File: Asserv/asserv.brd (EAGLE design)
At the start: 44.1 x 57.1 mm, 8 parts, among them IC1 7805TV

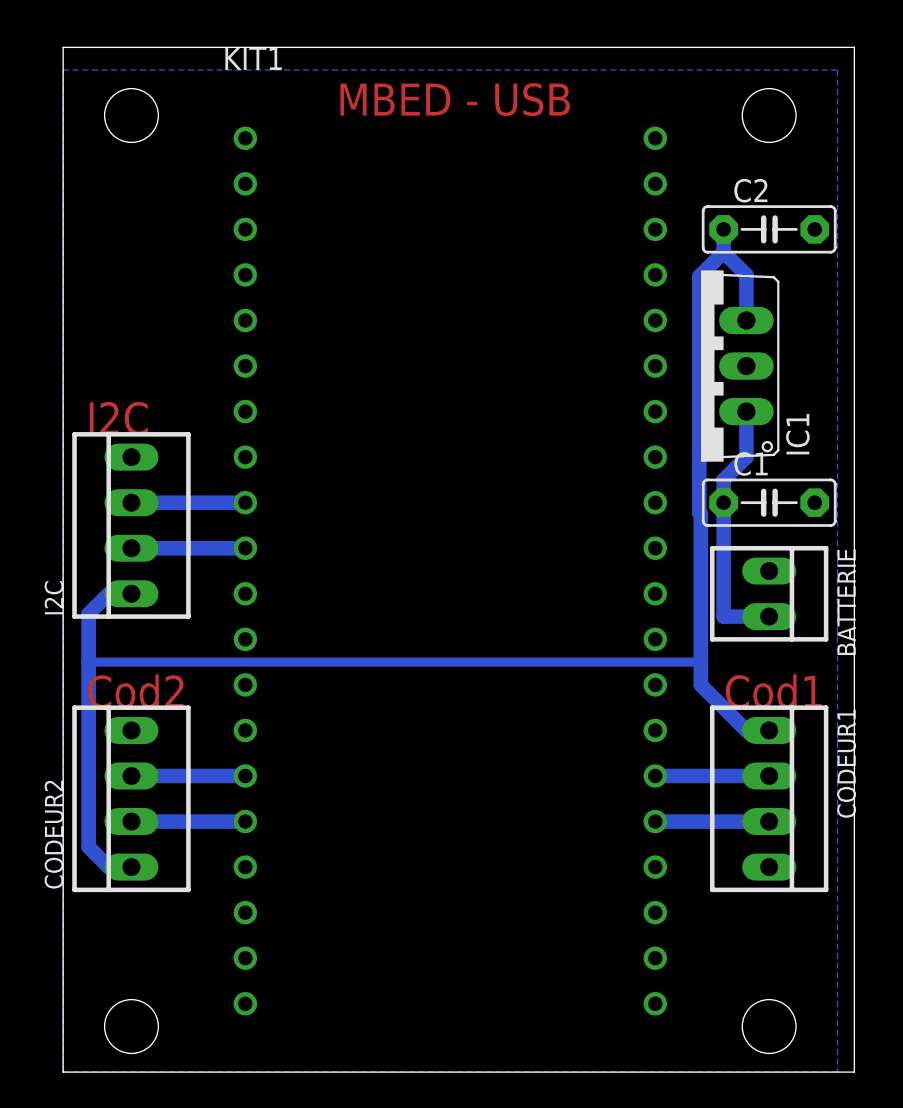
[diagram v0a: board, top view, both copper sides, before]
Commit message: ajout d'un i2c sur l'asserv et design de l'ia
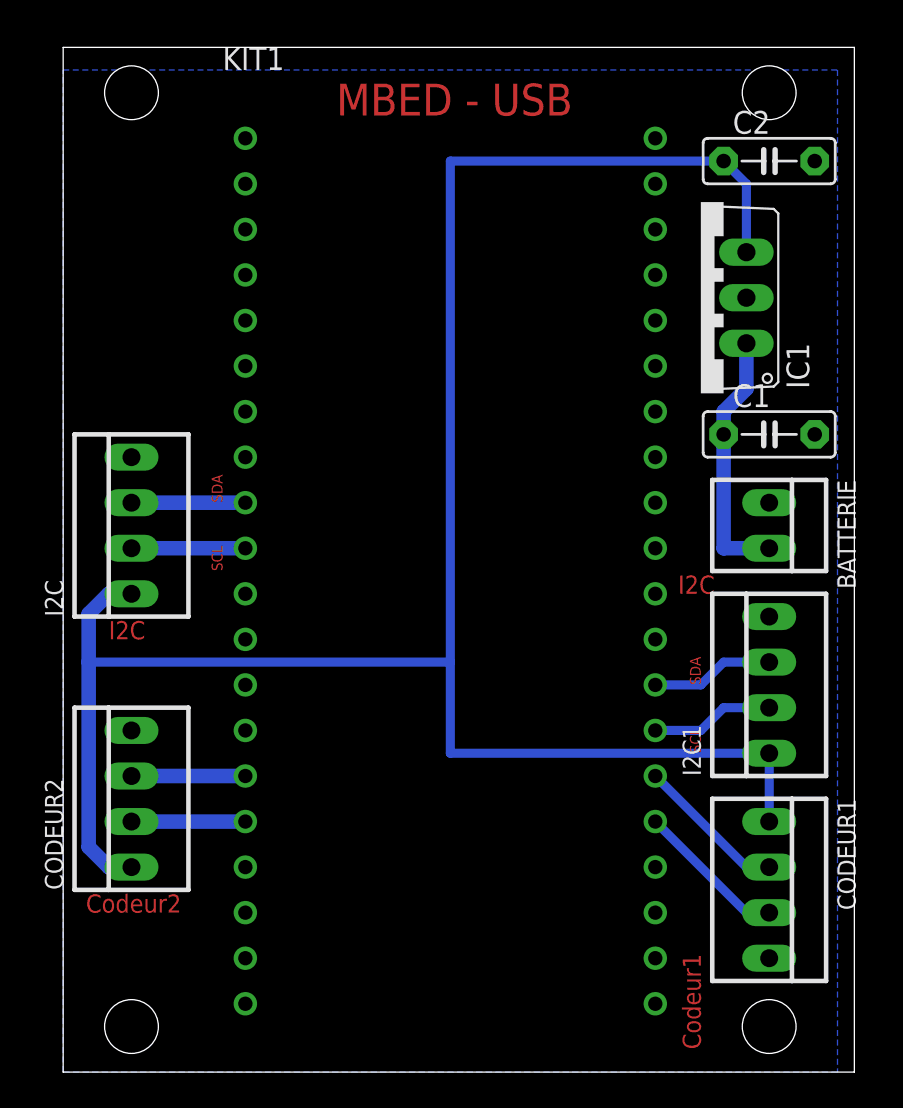
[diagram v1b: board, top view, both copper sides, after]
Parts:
- added I2C1: 22-23-2041, con-molex:22-23-2041
- moved CODEUR1 5.08 mm to (39.4, 10.2)
- moved C1 3.81 mm to (39.4, 35.6)
- moved IC1 3.81 mm to (35.6, 43.2)
- moved BATTERIE 3.81 mm to (39.4, 30.5)
- moved C2 3.81 mm to (39.4, 50.8)
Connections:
- new net N$2: I2C1.2, KIT1.P$27
- new net N$3: I2C1.3, KIT1.P$28
- net GND: now also I2C1.4
- net VCC: now also I2C1.1
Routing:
- net VCC: track 88.0 -> 114.3 mm
- net N$3: track 0.00 -> 6.88 mm
- net N$2: track 0.00 -> 6.88 mm
- net N$9: track 6.35 -> 8.45 mm
- net N$10: track 6.35 -> 8.45 mm
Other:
- board text added: "Codeur1"
- board text added: "Codeur2"
- board text added: "SCL"
- board text added: "SDA"
- board text removed: "Cod1"
- board text removed: "Cod2"

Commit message: lidar + reset mbed + trou ax12
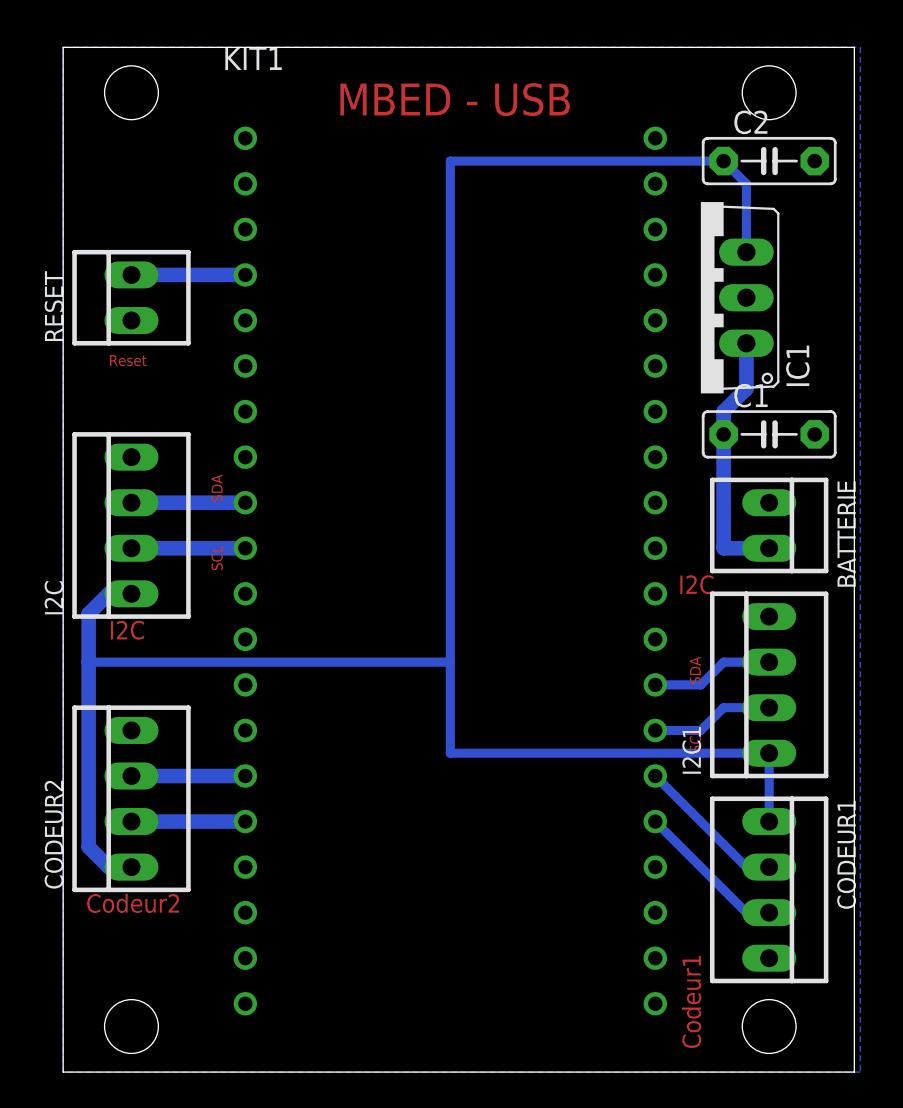
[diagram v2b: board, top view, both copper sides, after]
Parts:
- added RESET: 22-23-2021, con-molex:22-23-2021
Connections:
- removed net NR: KIT1.NR
- new net N$4: KIT1.NR, RESET.2
- net GND: now also RESET.1
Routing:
- net N$4: track 0.00 -> 6.35 mm
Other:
- board text added: "Reset"
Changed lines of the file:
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@@
 <?xml version="1.0" encoding="utf-8"?>
 <!DOCTYPE eagle SYSTEM "eagle.dtd">
-<eagle version="8.6.3">
+<eagle version="9.3.0">
 <drawing>
 <settings>
@@
 <text x="35.56" y="17.78" size="0.6096" layer="1" rot="R90">SCL</text>
 <text x="34.29" y="26.67" size="1.016" layer="1">I2C</text>
+<text x="2.54" y="39.37" size="0.6096" layer="1">Reset</text>
 </plain>
 <attributes>
@@
 <param name="checkStop" value="0"/>
 <param name="checkValues" value="0"/>
+<param name="checkNames" value="1"/>
+<param name="checkWireStubs" value="1"/>
+<param name="checkPolygonWidth" value="0"/>
 <param name="useDiameter" value="13"/>
 <param name="maxErrors" value="50"/>
@@
 </autorouter>
 <elements>
-<element name="BATTERIE" library="con-molex" library_urn="urn:adsk.eagle:library:165" package="22-23-2021" value="22-23-2021" x="39.37" y="30.48" rot="R270">
+<element name="BATTERIE" library="con-molex" library_urn="urn:adsk.eagle:library:165" package="22-23-2021" value="22-23-2021" x="39.37" y="30.48" smashed="yes" rot="R270">
 <attribute name="MF" value="MOLEX" x="39.37" y="30.48" size="1.778" layer="27" rot="R270" display="off"/>
 <attribute name="MPN" value="22-23-2021" x="39.37" y="30.48" size="1.778" layer="27" rot="R270" display="off"/>
+<attribute name="NAME" x="43.18" y="33.02" size="1.016" layer="25" ratio="10" rot="R270"/>
 <attribute name="OC_FARNELL" value="1462926" x="39.37" y="30.48" size="1.778" layer="27" rot="R270" display="off"/>
 <attribute name="OC_NEWARK" value="25C3832" x="39.37" y="30.48" size="1.778" layer="27" rot="R270" display="off"/>
-</element>
-<element name="C1" library="capacitor-wima" library_urn="urn:adsk.eagle:library:116" package="C5B2.5" value="0.33uF" x="39.37" y="35.56"/>
-<element name="C2" library="capacitor-wima" library_urn="urn:adsk.eagle:library:116" package="C5B2.5" value="0.1uF" x="39.37" y="50.8"/>
-<element name="CODEUR1" library="con-molex" library_urn="urn:adsk.eagle:library:165" package="22-23-2041" value="22-23-2041" x="39.37" y="10.16" rot="R270">
+<attribute name="VALUE" x="34.29" y="33.02" size="1.016" layer="27" ratio="10" rot="R270"/>
+</element>
+<element name="C1" library="capacitor-wima" library_urn="urn:adsk.eagle:library:116" package="C5B2.5" value="0.33uF" x="39.37" y="35.56" smashed="yes">
+<attribute name="NAME" x="37.338" y="37.084" size="1.27" layer="25" ratio="10"/>
+<attribute name="VALUE" x="37.338" y="32.766" size="1.27" layer="27" ratio="10"/>
+</element>
+<element name="C2" library="capacitor-wima" library_urn="urn:adsk.eagle:library:116" package="C5B2.5" value="0.1uF" x="39.37" y="50.8" smashed="yes">
+<attribute name="NAME" x="37.338" y="52.324" size="1.27" layer="25" ratio="10"/>
+<attribute name="VALUE" x="37.338" y="48.006" size="1.27" layer="27" ratio="10"/>
+</element>
+<element name="CODEUR1" library="con-molex" library_urn="urn:adsk.eagle:library:165" package="22-23-2041" value="22-23-2041" x="39.37" y="10.16" smashed="yes" rot="R270">
 <attribute name="MF" value="MOLEX" x="39.37" y="10.16" size="1.778" layer="27" rot="R270" display="off"/>
 <attribute name="MPN" value="22-23-2041" x="39.37" y="10.16" size="1.778" layer="27" rot="R270" display="off"/>
+<attribute name="NAME" x="43.18" y="15.24" size="1.016" layer="25" ratio="10" rot="R270"/>
 <attribute name="OC_FARNELL" value="1462920" x="39.37" y="10.16" size="1.778" layer="27" rot="R270" display="off"/>
 <attribute name="OC_NEWARK" value="38C0355" x="39.37" y="10.16" size="1.778" layer="27" rot="R270" display="off"/>
-</element>
-<element name="CODEUR2" library="con-molex" library_urn="urn:adsk.eagle:library:165" package="22-23-2041" value="22-23-2041" x="3.81" y="15.24" rot="R90">
+<attribute name="VALUE" x="34.29" y="15.24" size="1.016" layer="27" ratio="10" rot="R270"/>
+</element>
+<element name="CODEUR2" library="con-molex" library_urn="urn:adsk.eagle:library:165" package="22-23-2041" value="22-23-2041" x="3.81" y="15.24" smashed="yes" rot="R90">
 <attribute name="MF" value="MOLEX" x="3.81" y="15.24" size="1.778" layer="27" rot="R90" display="off"/>
 <attribute name="MPN" value="22-23-2041" x="3.81" y="15.24" size="1.778" layer="27" rot="R90" display="off"/>
+<attribute name="NAME" x="0" y="10.16" size="1.016" layer="25" ratio="10" rot="R90"/>
 <attribute name="OC_FARNELL" value="1462920" x="3.81" y="15.24" size="1.778" layer="27" rot="R90" display="off"/>
 <attribute name="OC_NEWARK" value="38C0355" x="3.81" y="15.24" size="1.778" layer="27" rot="R90" display="off"/>
-</element>
-<element name="I2C" library="con-molex" library_urn="urn:adsk.eagle:library:165" package="22-23-2041" value="22-23-2041" x="3.81" y="30.48" rot="R90">
+<attribute name="VALUE" x="8.89" y="10.16" size="1.016" layer="27" ratio="10" rot="R90"/>
+</element>
+<element name="I2C" library="con-molex" library_urn="urn:adsk.eagle:library:165" package="22-23-2041" value="22-23-2041" x="3.81" y="30.48" smashed="yes" rot="R90">
 <attribute name="MF" value="MOLEX" x="3.81" y="30.48" size="1.778" layer="27" rot="R90" display="off"/>
 <attribute name="MPN" value="22-23-2041" x="3.81" y="30.48" size="1.778" layer="27" rot="R90" display="off"/>
+<attribute name="NAME" x="0" y="25.4" size="1.016" layer="25" ratio="10" rot="R90"/>
 <attribute name="OC_FARNELL" value="1462920" x="3.81" y="30.48" size="1.778" layer="27" rot="R90" display="off"/>
 <attribute name="OC_NEWARK" value="38C0355" x="3.81" y="30.48" size="1.778" layer="27" rot="R90" display="off"/>
-</element>
-<element name="IC1" library="linear" library_urn="urn:adsk.eagle:library:262" package="TO220V" value="7805TV" x="35.56" y="43.18" rot="R90"/>
-<element name="KIT1" library="MBED_v2.1" package="MBED-KIT" value="MBED_NXP_LPC1768" x="21.59" y="27.94">
+<attribute name="VALUE" x="8.89" y="25.4" size="1.016" layer="27" ratio="10" rot="R90"/>
+</element>
+<element name="IC1" library="linear" library_urn="urn:adsk.eagle:library:262" package="TO220V" value="7805TV" x="35.56" y="43.18" smashed="yes" rot="R90">
+<attribute name="NAME" x="41.6052" y="38.1" size="1.27" layer="25" ratio="10" rot="R90"/>
+<attribute name="VALUE" x="43.18" y="38.1" size="1.27" layer="27" ratio="10" rot="R90"/>
+</element>
+<element name="KIT1" library="MBED_v2.1" package="MBED-KIT" value="MBED_NXP_LPC1768" x="21.59" y="27.94" smashed="yes">
 <attribute name="ARM" value="" x="21.59" y="27.94" size="1.778" layer="27" display="off"/>
-</element>
-<element name="I2C1" library="con-molex" library_urn="urn:adsk.eagle:library:165" package="22-23-2041" value="22-23-2041" x="39.37" y="21.59" rot="R90">
+<attribute name="NAME" x="8.89" y="55.88" size="1.27" layer="25"/>
+</element>
+<element name="I2C1" library="con-molex" library_urn="urn:adsk.eagle:library:165" package="22-23-2041" value="22-23-2041" x="39.37" y="21.59" smashed="yes" rot="R90">
 <attribute name="MF" value="MOLEX" x="39.37" y="21.59" size="1.778" layer="27" rot="R90" display="off"/>
 <attribute name="MPN" value="22-23-2041" x="39.37" y="21.59" size="1.778" layer="27" rot="R90" display="off"/>
+<attribute name="NAME" x="35.56" y="16.51" size="1.016" layer="25" ratio="10" rot="R90"/>
 <attribute name="OC_FARNELL" value="1462920" x="39.37" y="21.59" size="1.778" layer="27" rot="R90" display="off"/>
 <attribute name="OC_NEWARK" value="38C0355" x="39.37" y="21.59" size="1.778" layer="27" rot="R90" display="off"/>
+<attribute name="VALUE" x="44.45" y="16.51" size="1.016" layer="27" ratio="10" rot="R90"/>
+</element>
+<element name="RESET" library="con-molex" library_urn="urn:adsk.eagle:library:165" package="22-23-2021" value="22-23-2021" x="3.81" y="43.18" smashed="yes" rot="R90">
+<attribute name="MF" value="MOLEX" x="-8.89" y="35.56" size="1.778" layer="27" rot="R90" display="off"/>
+<attribute name="MPN" value="22-23-2021" x="-8.89" y="35.56" size="1.778" layer="27" rot="R90" display="off"/>
+<attribute name="NAME" x="0" y="40.64" size="1.016" layer="25" ratio="10" rot="R90"/>
+<attribute name="OC_FARNELL" value="1462926" x="-8.89" y="35.56" size="1.778" layer="27" rot="R90" display="off"/>
+<attribute name="OC_NEWARK" value="25C3832" x="-8.89" y="35.56" size="1.778" layer="27" rot="R90" display="off"/>
+<attribute name="VALUE" x="8.89" y="40.64" size="1.016" layer="27" ratio="10" rot="R90"/>
 </element>
 </elements>
@@
 <signal name="VB">
 <contactref element="KIT1" pad="VB"/>
-</signal>
-<signal name="NR">
-<contactref element="KIT1" pad="NR"/>
 </signal>
 <signal name="VU">
@@
 <polygon width="0.508" layer="16">
 <vertex x="0" y="0"/>
-<vertex x="0" y="55.88"/>
-<vertex x="43.18" y="55.88"/>
-<vertex x="43.18" y="0"/>
+<vertex x="0" y="57.15"/>
+<vertex x="44.45" y="57.15"/>
+<vertex x="44.45" y="0"/>
 </polygon>
 <contactref element="I2C1" pad="4"/>
+<contactref element="RESET" pad="1"/>
 </signal>
 <signal name="VCC">
@@
 <wire x1="35.56" y1="21.59" x2="33.02" y2="21.59" width="0.508" layer="16"/>
 </signal>
+<signal name="N$4">
+<contactref element="KIT1" pad="NR"/>
+<contactref element="RESET" pad="2"/>
+<wire x1="3.81" y1="44.45" x2="10.16" y2="44.45" width="0.8128" layer="16"/>
+</signal>
 </signals>
+<mfgpreviewcolors>
+<mfgpreviewcolor name="soldermaskcolor" color="0xC8008000"/>
+<mfgpreviewcolor name="silkscreencolor" color="0xFFFEFEFE"/>
+<mfgpreviewcolor name="backgroundcolor" color="0xFF282828"/>
+<mfgpreviewcolor name="coppercolor" color="0xFFFFBF00"/>
+<mfgpreviewcolor name="substratecolor" color="0xFF786E46"/>
+</mfgpreviewcolors>
 </board>
 </drawing>
